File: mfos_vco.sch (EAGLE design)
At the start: 60 parts, among them IC1 TL072P, IC2 TL072P, IC3 TL072P, IC4 LM394N, U1 POWER, U2 2N5457

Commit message: thicker traces and fewer jumps
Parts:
- R24: device rcl:R-US_0207/7 -> rcl:R-US_0207/5V
- R27: device rcl:R-US_0309/12 -> rcl:R-US_0309/10
- TEMPCO: device rcl:R-US_0207/2V -> rcl:R-US_0309/12
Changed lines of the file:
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@@
 <part name="P+3" library="supply1" deviceset="+12V" device=""/>
 <part name="C1" library="rcl" deviceset="C-US" device="050-024X044" value="100pF"/>
-<part name="TEMPCO" library="rcl" deviceset="R-US_" device="0207/2V" value="2k"/>
+<part name="TEMPCO" library="rcl" deviceset="R-US_" device="0309/12" value="2k"/>
 <part name="HIGH_FREQ_TRIM" library="pot" deviceset="TRIM_US-" device="B64Y" value="100k"/>
 <part name="R15" library="rcl" deviceset="R-US_" device="0207/7" value="4k7"/>
@@
 <part name="P+6" library="supply1" deviceset="+12V" device=""/>
 <part name="GND8" library="supply1" deviceset="GND" device=""/>
-<part name="R24" library="rcl" deviceset="R-US_" device="0207/7" value="100k"/>
+<part name="R24" library="rcl" deviceset="R-US_" device="0207/5V" value="100k"/>
 <part name="R25" library="rcl" deviceset="R-US_" device="0207/7" value="18k"/>
 <part name="P-5" library="supply1" deviceset="-12V" device=""/>
@@
 <part name="IC3" library="linear" deviceset="TL072" device="P"/>
 <part name="R9" library="pot" deviceset="TRIM_US-" device="B64Y" value="10k"/>
-<part name="R27" library="rcl" deviceset="R-US_" device="0309/12" value="100k"/>
+<part name="R27" library="rcl" deviceset="R-US_" device="0309/10" value="100k"/>
 <part name="P+8" library="supply1" deviceset="+12V" device=""/>
 <part name="GND14" library="supply1" deviceset="GND" device=""/>

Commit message: molex
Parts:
- removed C8, C9: 10uF, rcl:CPOL-USB45181A
- removed JP1: (no value), SparkFun-Connectors:M05LOCK_LONGPADS
- removed U1: POWER, eurorack:POWER
- added C11, C12: 10u, rcl:CPOL-USB45181A
- added C13, C14: 100n, rcl:C-US050-024X044
- added PWR1: POWER, eurorack:POWER
- added U$1, U$2: FB, adafruit:FB
- added X1: 22-23-2051, con-molex:22-23-2051
- CV2, CV3: value LSP10 -> 22-23-2021; device solpad:LSP10 -> con-molex:22-23-2021
- R26: device rcl:R-US_0207/7 -> rcl:R-US_0309/10
- R27: device rcl:R-US_0309/10 -> rcl:R-US_0207/10
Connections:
- new net N$38: PWR1.+12V, U$1.1
- new net N$39: PWR1.-12V, U$2.1
- net +12V: now also C11.+, C13.1, U$1.2, X1-3.S; no longer C8.+, JP1.3, U1.+12V
- net -12V: now also C12.-, C14.2, U$2.2, X1-1.S; no longer C9.-, JP1.1, U1.-12V
- net GND: now also CV2-2.S, CV3-2.S, X1-2.S; no longer C8.-, C9.+, JP1.2, U1.GND
- net N$11: now also PWR1.CV; no longer U1.CV
- net N$18: now also CV2-1.S; no longer CV2.MP
- net N$19: now also CV3-1.S; no longer CV3.MP
- net N$26: now also C11.-, C12.+, C13.2, C14.1, PWR1.GND
- net N$33: now also X1-4.S; no longer JP1.4
- net N$35: now also X1-5.S; no longer JP1.5
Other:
- moved on the sheet: IC3B, R17, R18, RAMP

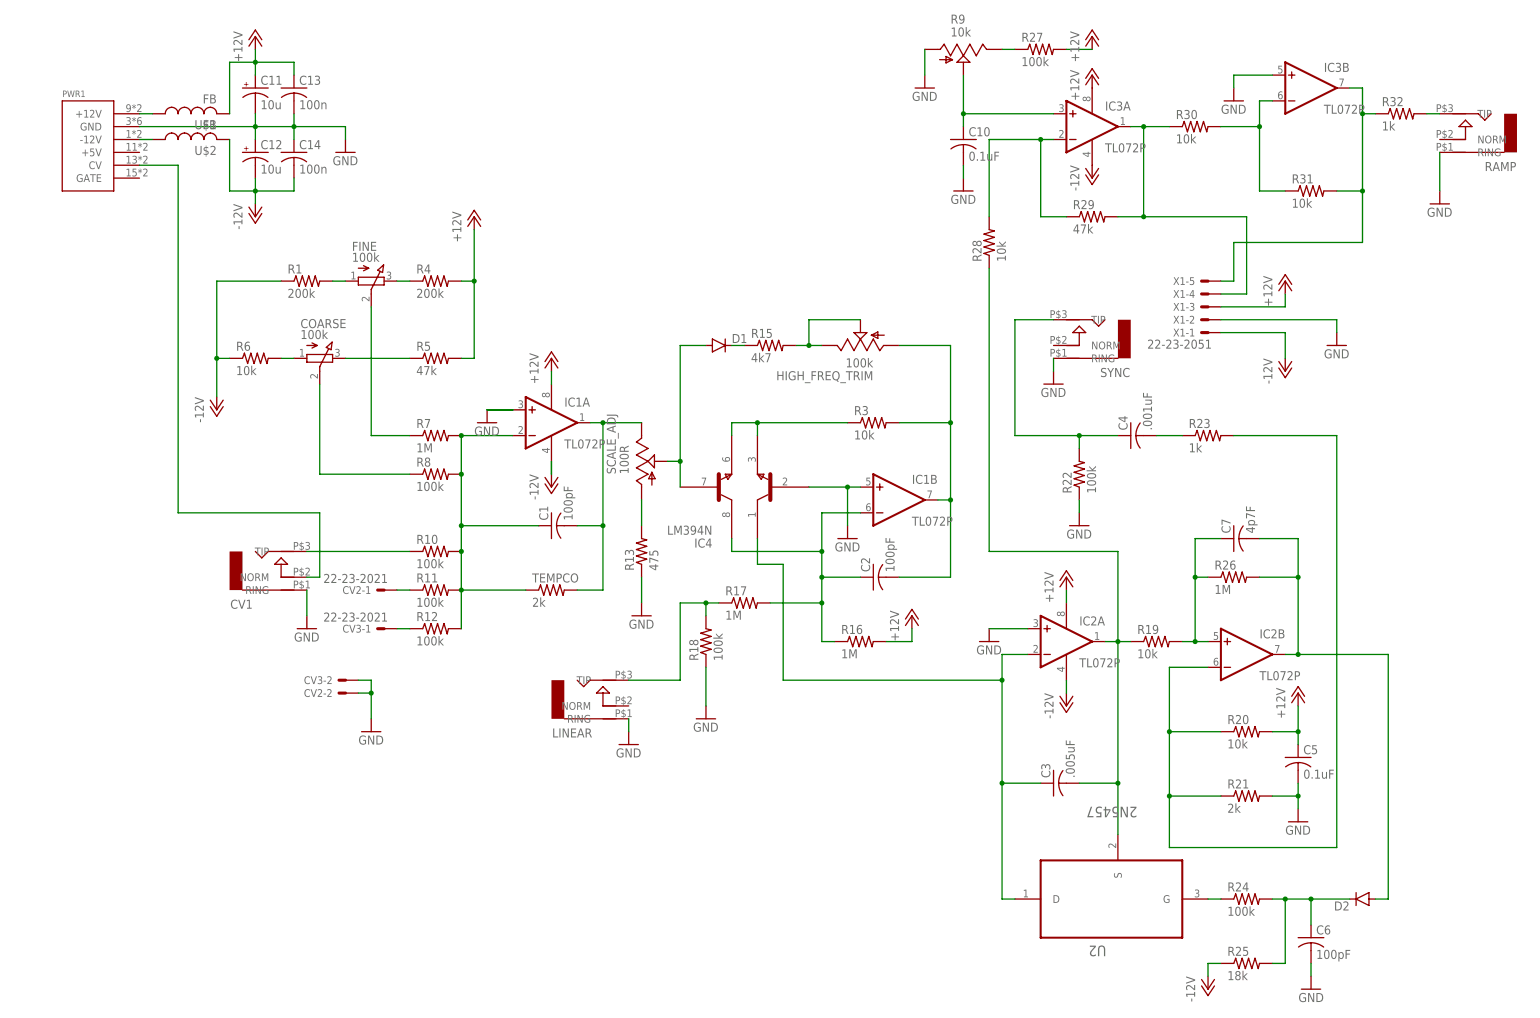
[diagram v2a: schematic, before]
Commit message: corrected separate ground signals and manually routed
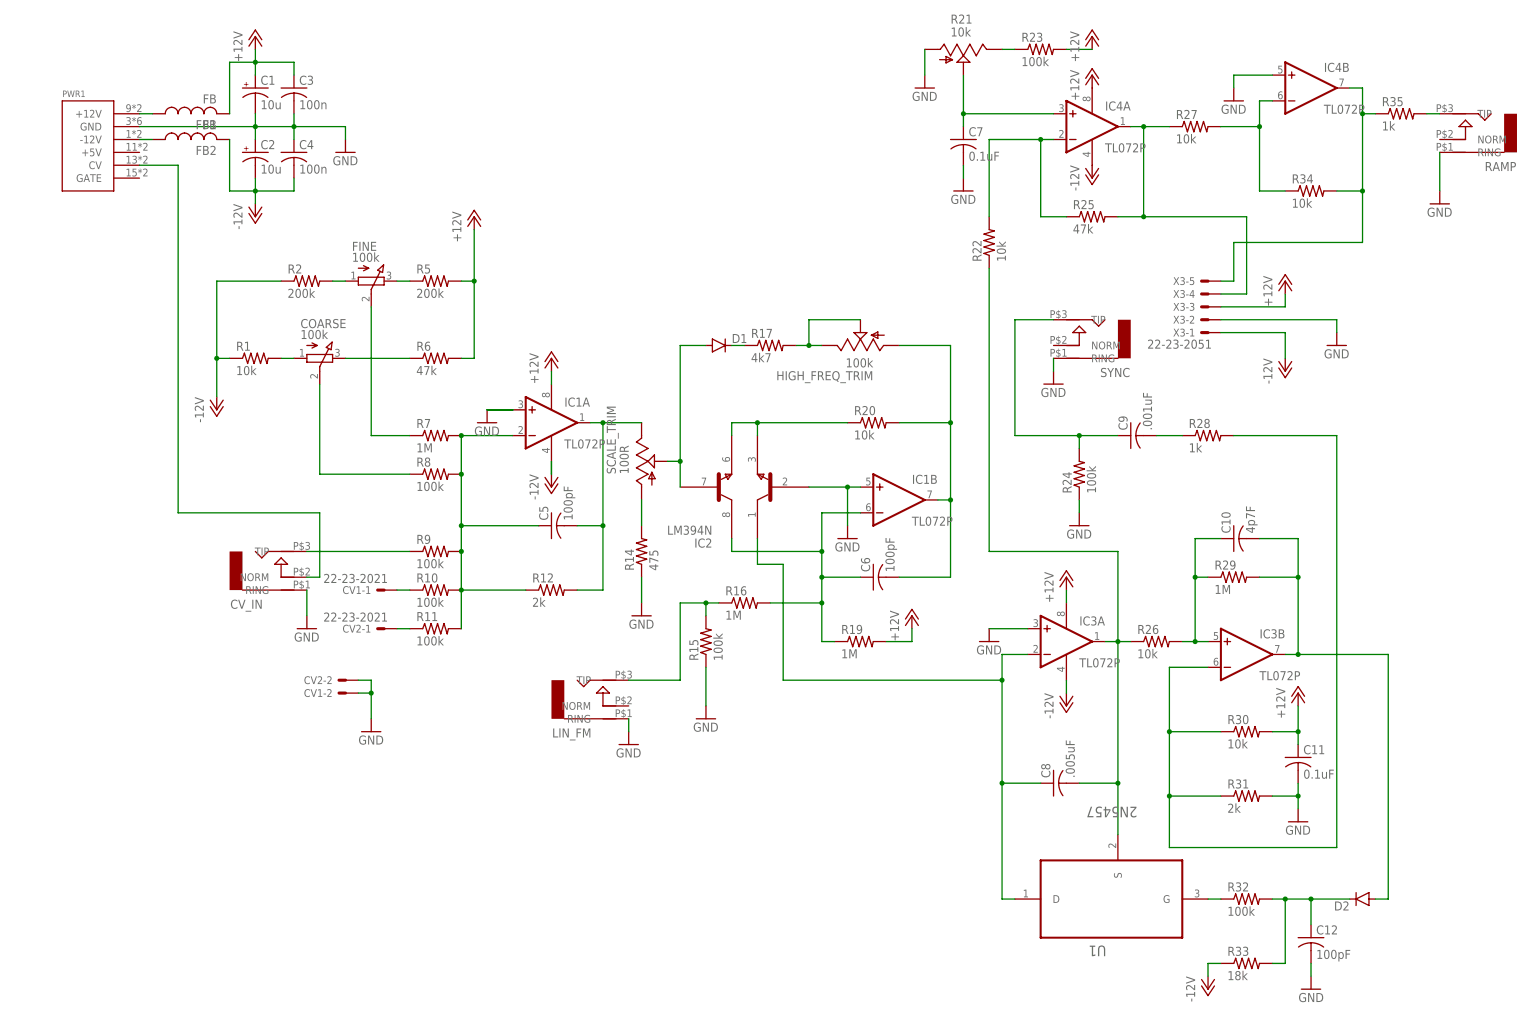
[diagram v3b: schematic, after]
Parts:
- removed C13, C14: 100n, rcl:C-US050-024X044
- removed CV3: 22-23-2021, con-molex:22-23-2021
- removed R18: 100k, rcl:R-US_0207/7
- removed R3: 10k, rcl:R-US_0207/7
- removed R4: 200k, rcl:R-US_0207/7
- removed TEMPCO: 2k, rcl:R-US_0309/12
- added C8: .005uF, rcl:C-US050-024X044
- added C9: .001uF, rcl:C-US050-024X044
- added CV_IN: AUDIO-JACK, erthenvar:AUDIO-JACK
- added R2: 200k, rcl:R-US_0207/7
- added R33: 18k, rcl:R-US_0207/7
- added R34: 10k, rcl:R-US_0207/7
- added R35: 1k, rcl:R-US_0207/7
- C1, C2: value 100pF -> 10u; device rcl:C-US050-024X044 -> rcl:CPOL-USB45181A
- C10: value 0.1uF -> 4p7F
- C11: value 10u -> 0.1uF; device rcl:CPOL-USB45181A -> rcl:C-US050-024X044
- C12: value 10u -> 100pF; device rcl:CPOL-USB45181A -> rcl:C-US050-024X044
- C3: value .005uF -> 100n
- C4: value .001uF -> 100n
- C5: value 0.1uF -> 100pF
- C7: value 4p7F -> 0.1uF
- CV1: value AUDIO-JACK -> 22-23-2021; device erthenvar:AUDIO-JACK -> con-molex:22-23-2021
- IC2: value TL072P -> LM394N; device linear:TL072P -> synthdiy:LM394N
- IC4: value LM394N -> TL072P; device synthdiy:LM394N -> linear:TL072P
- R1: value 200k -> 10k
- R12: value 100k -> 2k
- R15: value 4k7 -> 100k
- R17: value 1M -> 4k7
- R19: value 10k -> 1M
- R21: value 2k -> 10k; device rcl:R-US_0207/7 -> pot:TRIM_US-B64Y
- R22: value 100k -> 10k
- R23: value 1k -> 100k; device rcl:R-US_0207/7 -> rcl:R-US_0207/10
- R24: device rcl:R-US_0207/5V -> rcl:R-US_0207/7
- R25: value 18k -> 47k
- R26: value 1M -> 10k; device rcl:R-US_0309/10 -> rcl:R-US_0207/7
- R27: value 100k -> 10k; device rcl:R-US_0207/10 -> rcl:R-US_0207/7
- R28: value 10k -> 1k
- R29: value 47k -> 1M
- R31: value 10k -> 2k
- R32: value 1k -> 100k
- R5: value 47k -> 200k
- R6: value 10k -> 47k
- R9: value 10k -> 100k; device pot:TRIM_US-B64Y -> rcl:R-US_0207/7
- renumbered LINEAR to LIN_FM, R13 to R14, SCALE_ADJ to SCALE_TRIM, U$1 to FB1, U$2 to FB2, U2 to U1, X1 to X3
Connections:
- removed net N$19 (its old number): CV3-1.S, R12.1
- new net N$18: CV1-1.S, R10.1
- net +12V: now also C1.+, C11.1, C3.1, IC4P.V+, R19.2, R23.2, R30.2, R6.2; no longer C11.+, C13.1, C5.1, IC2P.V+, R16.2, R20.2, R27.2, R4.2
- net -12V: now also C2.-, C4.2, IC4P.V-, R2.1, R33.1; no longer C12.-, C14.2, IC2P.V-, R25.1, R6.1
- net GND: now also C1.-, C11.2, C12.2, C2.+, C3.2, C4.1, C7.2, CV1-2.S, CV_IN.RING, IC2.B1, IC3A.+IN, IC4B.+IN, PWR1.GND, R15.1, R21.A, R24.1, R31.2; no longer C10.2, C5.2, C6.2, CV1.RING, CV3-2.S, IC2A.+IN, IC3B.+IN, IC4.B1, R18.1, R21.2, R22.1, R9.A
- net N$1: now also R1.2; no longer R6.2
- net N$10: now also C5.1, R12.1, R9.2; no longer C1.1, R12.2, TEMPCO.1
- net N$11: now also CV_IN.NORM; no longer CV1.NORM
- net N$12: now also IC2.E1, IC2.E2, R20.1; no longer IC4.E1, IC4.E2, R3.1
- net N$14: now also R17.2; no longer R15.2
- net N$15: now also R17.1; no longer R15.1
- net N$16: now also C6.2, R20.2; no longer C2.2, R3.2
- net N$17: now also CV_IN.TIP, R9.1; no longer CV1.TIP, R10.1
- net N$2: now also R2.2; no longer R1.2
- net N$20: now also R15.2, R16.1; no longer R17.1, R18.2
- net N$21: now also C8.2, IC3A.OUT, R22.1, R26.1; no longer C3.2, IC2A.OUT, R19.1, R28.1
- net N$22: now also C10.1, IC3B.+IN, R26.2, R29.1; no longer C7.1, IC2B.+IN, R19.2, R26.1
- net N$23: now also C8.1, IC2.C1, IC3A.-IN; no longer C3.1, IC2A.-IN, IC4.C1
- net N$24: now also C9.2, R28.1; no longer C4.2, R23.1
- net N$25: now also C9.1, R24.2; no longer C4.1, R22.2
- net N$26: now also IC3B.-IN, R28.2, R30.1, R31.1; no longer C11.-, C12.+, C13.2, C14.1, IC2B.-IN, PWR1.GND, R20.1, R21.1, R23.2
- net N$27: now also R21.E, R23.1; no longer R27.1, R9.E
- net N$28: now also C7.1, IC4A.+IN, R21.S; no longer C10.1, IC3A.+IN, R9.S
- net N$29: now also R32.1; no longer R24.1
- net N$3: now also R5.1; no longer R4.1
- net N$30: now also C10.2, IC3B.OUT, R29.2; no longer C7.2, IC2B.OUT, R26.2
- net N$31: now also IC4A.-IN, R22.2, R25.1; no longer IC3A.-IN, R28.2, R29.1
- net N$32: now also C12.1, R32.2, R33.2; no longer C6.1, R24.2, R25.2
- net N$33: now also IC4A.OUT, R25.2, R27.1; no longer IC3A.OUT, R29.2, R30.1
- net N$34: now also IC4B.-IN, R27.2, R34.1; no longer IC3B.-IN, R30.2, R31.1
- net N$35: now also IC4B.OUT, R34.2, R35.1; no longer IC3B.OUT, R31.2, R32.1
- net N$36: now also R35.2; no longer R32.2
- net N$4: now also R6.1; no longer R5.1
- net N$40: now also C6.1, IC2.C2, R16.2, R19.1; no longer C2.1, IC4.C2, R16.1, R17.2
- net N$8: now also IC2.B2; no longer IC4.B2
- net N$9: now also C5.2, R12.2; no longer C1.2, TEMPCO.2
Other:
- moved on the sheet: C10, C3, C4, C5, C6, C7, CV2-1, CV2-2, IC3A, IC3B, R1, R10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

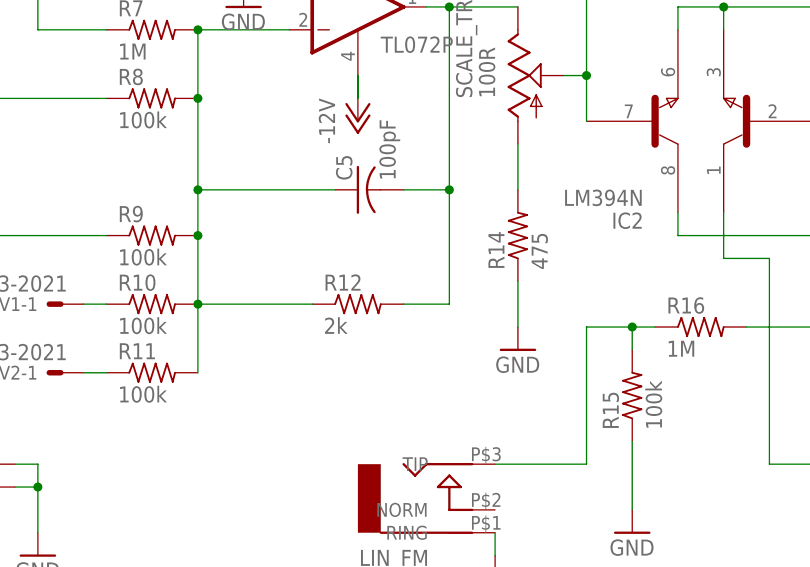
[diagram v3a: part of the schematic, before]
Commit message: routed manually with two jumpers
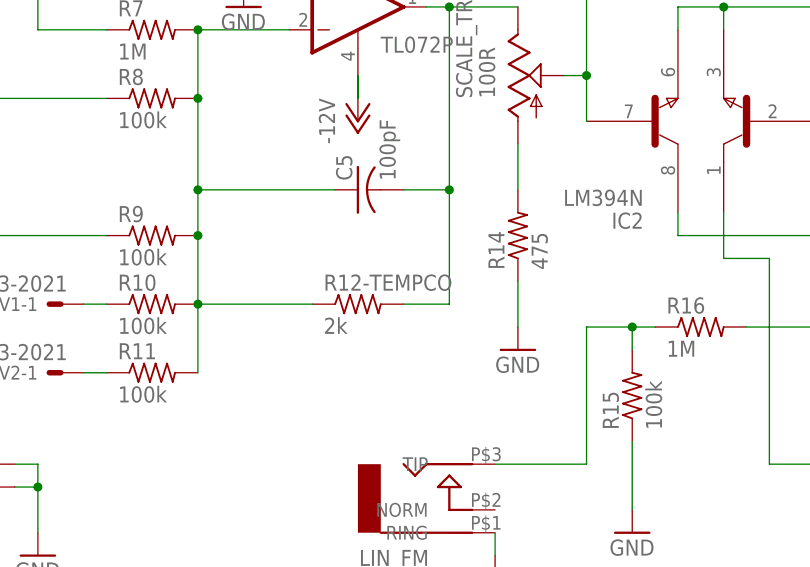
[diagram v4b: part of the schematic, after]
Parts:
- removed R12: 2k, rcl:R-US_0207/7
- added R12-TEMPCO: 2k, rcl:R-US_0207/2V
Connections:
- net N$10: now also R12-TEMPCO.1; no longer R12.1
- net N$9: now also R12-TEMPCO.2; no longer R12.2
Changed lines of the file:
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@@
 <part name="P+3" library="supply1" deviceset="+12V" device=""/>
 <part name="C5" library="rcl" deviceset="C-US" device="050-024X044" value="100pF"/>
-<part name="R12" library="rcl" deviceset="R-US_" device="0207/7" value="2k"/>
+<part name="R12-TEMPCO" library="rcl" deviceset="R-US_" device="0207/2V" value="2k"/>
 <part name="HIGH_FREQ_TRIM" library="pot" deviceset="TRIM_US-" device="B64Y" value="100k"/>
 <part name="R17" library="rcl" deviceset="R-US_" device="0207/7" value="4k7"/>
@@
 <instance part="P+3" gate="1" x="83.82" y="83.82"/>
 <instance part="C5" gate="G$1" x="83.82" y="50.8" rot="R90"/>
-<instance part="R12" gate="G$1" x="83.82" y="38.1"/>
+<instance part="R12-TEMPCO" gate="G$1" x="83.82" y="38.1"/>
 <instance part="HIGH_FREQ_TRIM" gate="G$1" x="144.78" y="86.36" rot="R90"/>
 <instance part="R17" gate="G$1" x="127" y="86.36"/>
@@
 <pinref part="SCALE_TRIM" gate="G$1" pin="E"/>
 <wire x1="101.6" y1="71.12" x2="93.98" y2="71.12" width="0.1524" layer="91"/>
-<pinref part="R12" gate="G$1" pin="2"/>
+<pinref part="R12-TEMPCO" gate="G$1" pin="2"/>
 <wire x1="93.98" y1="71.12" x2="91.44" y2="71.12" width="0.1524" layer="91"/>
 <wire x1="88.9" y1="38.1" x2="93.98" y2="38.1" width="0.1524" layer="91"/>
@@
 <wire x1="81.28" y1="50.8" x2="66.04" y2="50.8" width="0.1524" layer="91"/>
 <junction x="66.04" y="50.8"/>
-<pinref part="R12" gate="G$1" pin="1"/>
+<pinref part="R12-TEMPCO" gate="G$1" pin="1"/>
 <wire x1="78.74" y1="38.1" x2="66.04" y2="38.1" width="0.1524" layer="91"/>
 </segment>
